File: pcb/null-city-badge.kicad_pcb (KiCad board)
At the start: 2 copper layers, 113.3 x 118.1 mm, 144 parts, among them J1 USB_C_Receptacle_USB2.0_16P, J10 Conn_01x10_Pin, J11 Conn_Coaxial_Small, J12 Conn_01x07_Pin, J2 Conn_01x02_Pin, J3 Conn_01x06_Pin, J4 Conn_01x24_Socket, J5 Conn_Coaxial_Small, J6 Conn_01x06_Pin, J7 Conn_01x06_Pin, J8 Conn_01x06_Pin, J9 Conn_01x10_Pin, Q1 SS8050, Q2 SS8050, Q3 IRLML0030, Q4 AO3401A, Q5 SS8050, U1 ESP32-S3-WROOM-1, U10 TCA9534, U11 CORE1262-868M, U12 ME6211C33M5, U13 CC1101RGP, U14 ME6211C33M5, U2 CP2102N-Axx-xQFN28, U3 SE050C2HQ1_Z01SDZ, U4 MCP73831-2-MC, U5 ME6211C33M5, U6 ME6211C33M5, U7 NS4168, U8 74125, U9 ME6211C33M5, Y2 26Mhz

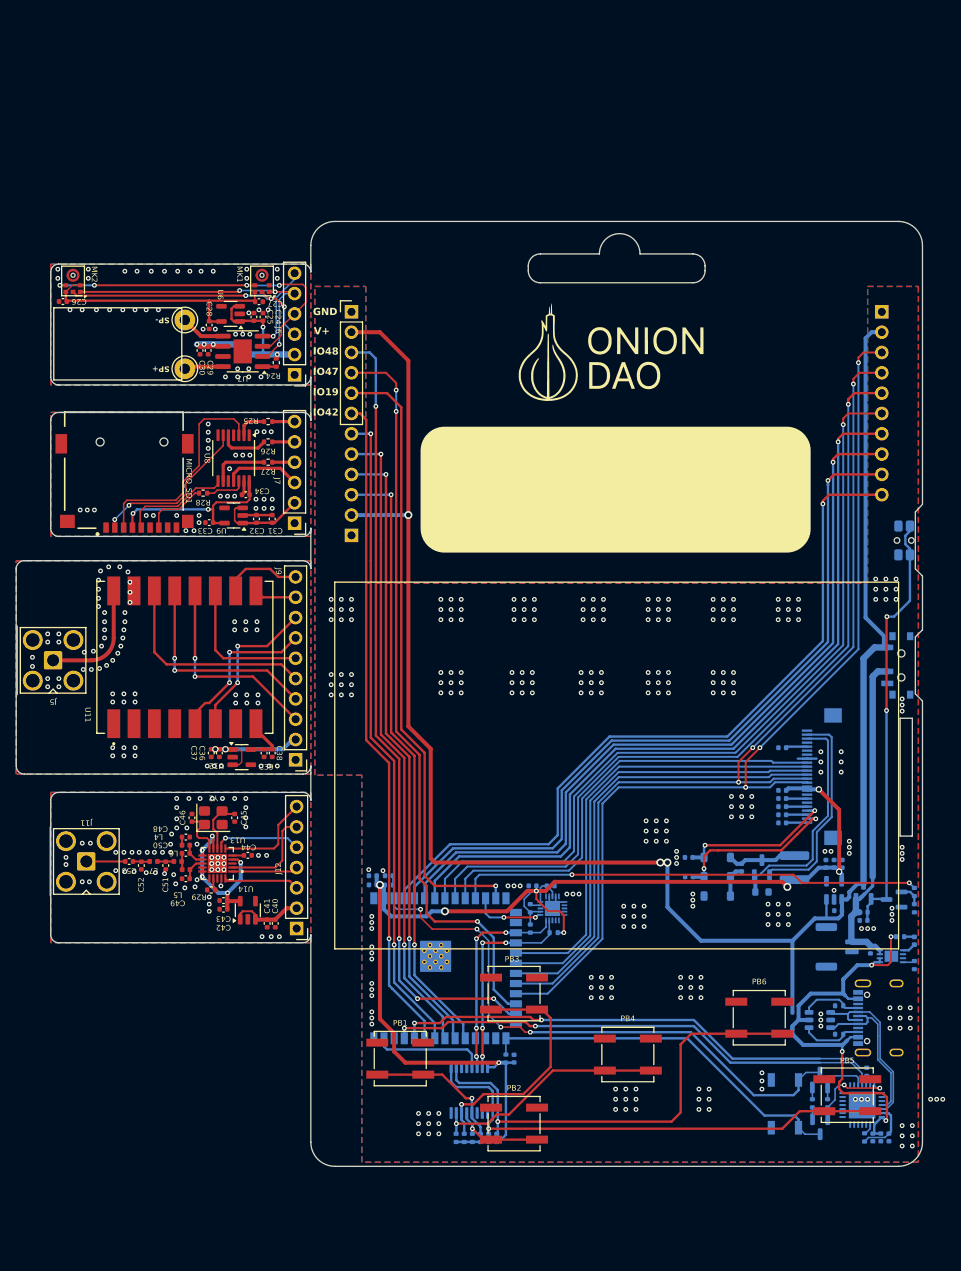
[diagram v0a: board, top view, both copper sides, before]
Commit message: feat: main board with sub ghz and audio modules, remove lora and sdcard
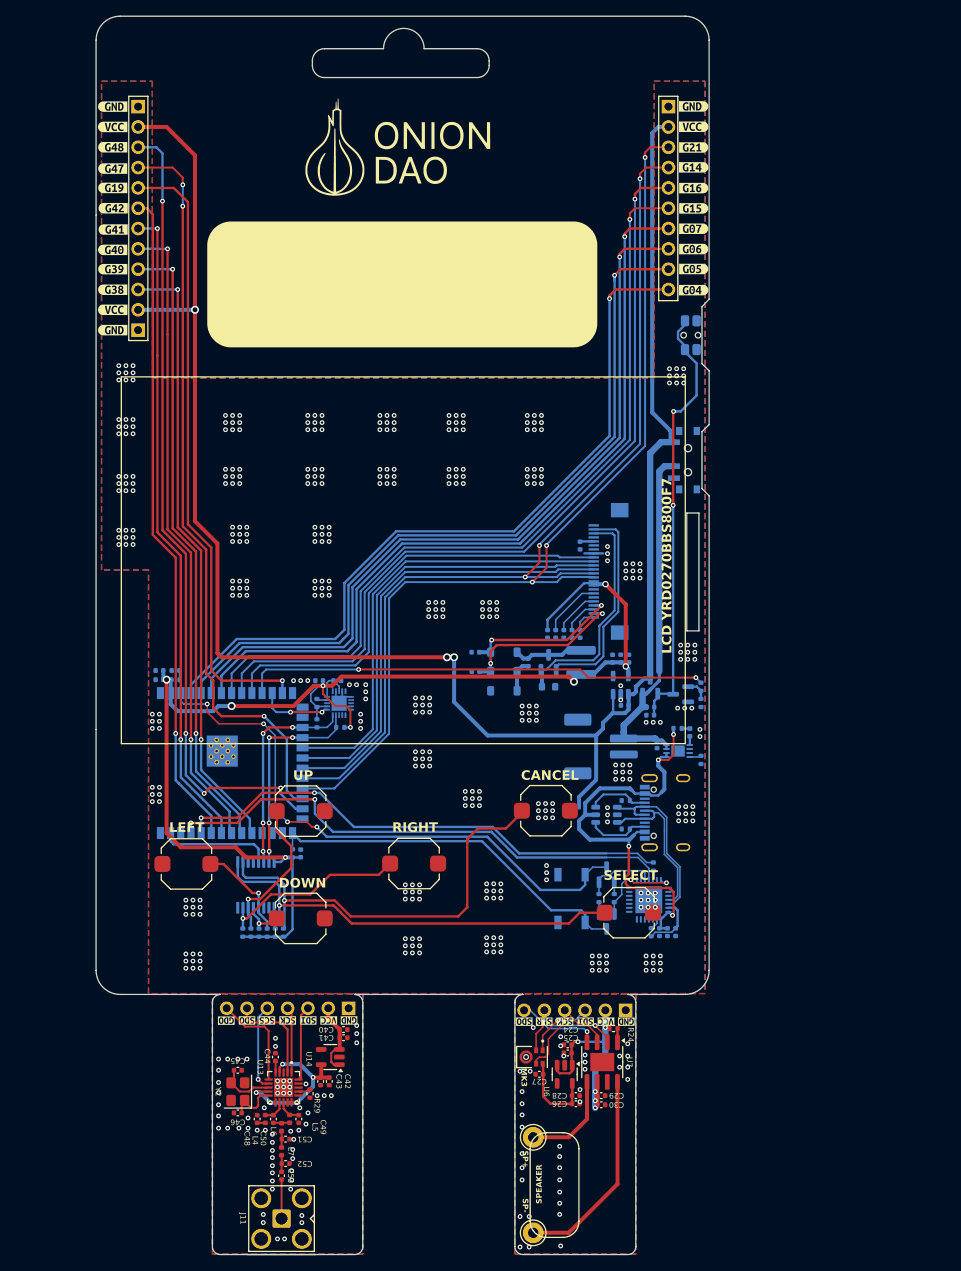
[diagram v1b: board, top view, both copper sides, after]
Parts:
- removed C31, C33, C36, C38: 10U, Capacitor_SMD:C_0402_1005Metric
- removed C32, C34, C37, C39: 100n, Capacitor_SMD:C_0402_1005Metric
- removed the G*** at (71.2, 89.4)
- removed the G*** at (74.4, 120.6)
- removed J5: Conn_Coaxial_Small, Connector_Coaxial:SMA_Amphenol_901-143_Horizontal
- removed J7: Conn_01x06_Pin, Connector_PinHeader_2.54mm:PinHeader_1x06_P2.54mm_Vertical
- removed J9: Conn_01x10_Pin, Connector_PinHeader_2.54mm:PinHeader_1x10_P2.54mm_Vertical
- removed MICRO_SD1: TF-01A, NIP_MOD:TF-01A
- removed MK1, MK2: ICS-43434, Sensor_Audio:InvenSense_ICS-43434-6_3.5x2.65mm
- removed R25, R26, R27, R28: R, Resistor_SMD:R_0402_1005Metric
- removed U11: CORE1262-868M, NIP_MOD:XCVR_CORE1262-868M
- removed U12, U9: ME6211C33M5, Package_TO_SOT_SMD:SOT-23-5
- removed U8: 74125, Package_SO:TSSOP-14_4.4x5mm_P0.65mm
- added G***: LOGO, NIP_LOGO:S_LOGO, B.Cu at (109.3, 56.0)
- added G***: LOGO, NIP_LOGO:S_LOGO_6, B.Cu at (125.6, 178.0)
- added G***: LOGO, NIP_LOGO:S_LOGO_6, B.Cu at (89.3, 173.5)
- added MK3: SPH0641LM4H-1, NIP_MOD:MIC_SPH0641LM4H-1, F.Cu at (123.7, 162.4)
- added kibuzzard-69D663AD: G***, kibuzzard-69D663AD, F.Cu at (144.6, 46.1)
- added kibuzzard-69D663C6: G***, kibuzzard-69D663C6, F.Cu at (144.6, 43.5)
- added kibuzzard-69D663C6: G***, kibuzzard-69D663C6, B.Cu at (72.0, 43.6)
- added kibuzzard-69D663C6: G***, kibuzzard-69D663C6, B.Cu at (136.1, 159.9)
- added kibuzzard-69D663C6: G***, kibuzzard-69D663C6, B.Cu at (72.0, 71.5)
- added kibuzzard-69D663C6: G***, kibuzzard-69D663C6, B.Cu at (101.4, 159.7)
- added kibuzzard-69D663D7: G***, kibuzzard-69D663D7, F.Cu at (144.6, 48.7)
- added kibuzzard-69D663E3: G***, kibuzzard-69D663E3, F.Cu at (144.6, 51.2)
- added kibuzzard-69D66402: G***, kibuzzard-69D66402, F.Cu at (144.6, 53.7)
- added kibuzzard-69D66408: G***, kibuzzard-69D66408, F.Cu at (144.6, 56.3)
- added kibuzzard-69D6643F: G***, kibuzzard-69D6643F, F.Cu at (144.6, 58.8)
- added kibuzzard-69D66453: G***, kibuzzard-69D66453, F.Cu at (144.6, 61.4)
- added kibuzzard-69D6645F: G***, kibuzzard-69D6645F, F.Cu at (144.6, 63.9)
- added kibuzzard-69D66465: G***, kibuzzard-69D66465, F.Cu at (144.6, 66.5)
- added kibuzzard-69D66565: G***, kibuzzard-69D66565, F.Cu at (72.0, 43.6)
- added kibuzzard-69D66565: G***, kibuzzard-69D66565, F.Cu at (72.0, 71.5)
- added kibuzzard-69D66565: G***, kibuzzard-69D66565, B.Cu at (144.6, 43.5)
- added kibuzzard-69D66580: G***, kibuzzard-69D66580, F.Cu at (72.0, 69.0)
- added kibuzzard-69D66580: G***, kibuzzard-69D66580, F.Cu at (72.0, 46.1)
- added kibuzzard-69D66580: G***, kibuzzard-69D66580, B.Cu at (144.6, 46.1)
- added kibuzzard-69D665BB: G***, kibuzzard-69D665BB, B.Cu at (144.6, 66.5)
- added kibuzzard-69D665D2: G***, kibuzzard-69D665D2, B.Cu at (144.6, 63.9)
- added kibuzzard-69D665E3: G***, kibuzzard-69D665E3, B.Cu at (144.6, 61.4)
- added kibuzzard-69D665EF: G***, kibuzzard-69D665EF, B.Cu at (144.6, 58.8)
- added kibuzzard-69D665FA: G***, kibuzzard-69D665FA, B.Cu at (144.6, 56.3)
- added kibuzzard-69D66608: G***, kibuzzard-69D66608, B.Cu at (144.6, 51.2)
- added kibuzzard-69D66615: G***, kibuzzard-69D66615, B.Cu at (144.6, 48.7)
- added kibuzzard-69D66624: G***, kibuzzard-69D66624, B.Cu at (144.6, 53.7)
- added kibuzzard-69D673B2: G***, kibuzzard-69D673B2, F.Cu at (72.0, 48.6)
- added kibuzzard-69D673C1: G***, kibuzzard-69D673C1, F.Cu at (72.0, 51.3)
- added kibuzzard-69D673C9: G***, kibuzzard-69D673C9, F.Cu at (72.0, 53.7)
- added kibuzzard-69D673D2: G***, kibuzzard-69D673D2, F.Cu at (72.1, 56.3)
- added kibuzzard-69D673D8: G***, kibuzzard-69D673D8, F.Cu at (72.1, 58.9)
- added kibuzzard-69D673DD: G***, kibuzzard-69D673DD, F.Cu at (72.0, 61.5)
- added kibuzzard-69D673E3: G***, kibuzzard-69D673E3, F.Cu at (72.0, 63.9)
- added kibuzzard-69D673EE: G***, kibuzzard-69D673EE, F.Cu at (72.0, 66.4)
- added kibuzzard-69D70112: G***, kibuzzard-69D70112, B.Cu at (98.9, 159.7)
- added kibuzzard-69D70112: G***, kibuzzard-69D70112, B.Cu at (133.6, 159.9)
- added kibuzzard-69D70112: G***, kibuzzard-69D70112, B.Cu at (72.0, 46.1)
- added kibuzzard-69D70126: G***, kibuzzard-69D70126, B.Cu at (72.0, 48.6)
- added kibuzzard-69D7012B: G***, kibuzzard-69D7012B, B.Cu at (72.0, 51.3)
- added kibuzzard-69D70130: G***, kibuzzard-69D70130, B.Cu at (72.0, 53.7)
- added kibuzzard-69D70134: G***, kibuzzard-69D70134, B.Cu at (72.1, 56.3)
- added kibuzzard-69D70141: G***, kibuzzard-69D70141, B.Cu at (72.1, 58.9)
- added kibuzzard-69D70146: G***, kibuzzard-69D70146, B.Cu at (72.0, 61.5)
- added kibuzzard-69D7014E: G***, kibuzzard-69D7014E, B.Cu at (72.0, 63.9)
- added kibuzzard-69D70154: G***, kibuzzard-69D70154, B.Cu at (72.0, 66.4)
- added kibuzzard-69D70186: G***, kibuzzard-69D70186, B.Cu at (72.0, 69.0)
- added kibuzzard-69D7A260: G***, kibuzzard-69D7A260, B.Cu at (88.7, 159.7)
- added kibuzzard-69D7A260: G***, kibuzzard-69D7A260, B.Cu at (123.4, 159.9)
- added kibuzzard-69D7A287: G***, kibuzzard-69D7A287, B.Cu at (128.5, 160.0)
- added kibuzzard-69D7A287: G***, kibuzzard-69D7A287, B.Cu at (93.8, 159.7)
- added kibuzzard-69D7A28C: G***, kibuzzard-69D7A28C, B.Cu at (131.1, 159.9)
- added kibuzzard-69D7A28C: G***, kibuzzard-69D7A28C, B.Cu at (96.3, 159.7)
- added kibuzzard-69D7A2FA: G***, kibuzzard-69D7A2FA, B.Cu at (126.0, 159.9)
- added kibuzzard-69D7A5EF: G***, kibuzzard-69D7A5EF, F.Cu at (125.9, 157.9)
- added kibuzzard-69D7A5F4: G***, kibuzzard-69D7A5F4, F.Cu at (123.5, 157.9)
- added kibuzzard-69D7A5F4: G***, kibuzzard-69D7A5F4, F.Cu at (88.8, 157.8)
- added kibuzzard-69D7A626: G***, kibuzzard-69D7A626, F.Cu at (93.9, 157.8)
- added kibuzzard-69D7A626: G***, kibuzzard-69D7A626, F.Cu at (128.5, 157.9)
- added kibuzzard-69D7A630: G***, kibuzzard-69D7A630, F.Cu at (96.5, 157.8)
- added kibuzzard-69D7A630: G***, kibuzzard-69D7A630, F.Cu at (131.1, 157.9)
- added kibuzzard-69D7A638: G***, kibuzzard-69D7A638, F.Cu at (99.0, 157.8)
- added kibuzzard-69D7A638: G***, kibuzzard-69D7A638, F.Cu at (133.7, 157.9)
- added kibuzzard-69D7A640: G***, kibuzzard-69D7A640, F.Cu at (136.2, 157.9)
- added kibuzzard-69D7A640: G***, kibuzzard-69D7A640, F.Cu at (101.6, 157.8)
- added kibuzzard-69D7D7AD: G***, kibuzzard-69D7D7AD, B.Cu at (86.2, 159.7)
- added kibuzzard-69D7D7BC: G***, kibuzzard-69D7D7BC, B.Cu at (91.2, 159.7)
- added kibuzzard-69D7D86C: G***, kibuzzard-69D7D86C, F.Cu at (91.3, 157.8)
- added kibuzzard-69D7D873: G***, kibuzzard-69D7D873, F.Cu at (86.2, 157.8)
- C2: value 1OOn -> 100n
- J12, J6: moved to B.Cu
- J2: footprint Connector_JST:JST_GH_SM02B-GHS-TB_1x02-1MP_P1.25mm_Horizontal -> Connector_JST:JST_PH_S2B-PH-SM4-TB_1x02-1MP_P2.00mm_Horizontal
- PB1, PB2, PB3, PB4, PB5, PB6: footprint Button_Switch_SMD:SW_SPST_B3SL-1002P -> Button_Switch_SMD:SW_Push_1TS009xxxx-xxxx-xxxx_6x6x5mm
- moved G*** 124.3 mm to (132.3, 179.0), turned to -90 degrees
- moved C26 119.0 mm to (129.9, 168.2), turned to 0 degrees
- moved TP1 116.5 mm to (124.6, 184.3)
- moved TP2 111.1 mm to (124.6, 172.4)
- moved C30 106.8 mm to (133.1, 168.3), turned to 0 degrees
- moved C28 106.7 mm to (129.9, 167.2), turned to 180 degrees
- moved C29 105.3 mm to (133.1, 167.2), turned to 0 degrees
- moved U6 103.8 mm to (128.5, 164.5), turned to -90 degrees
- moved C27 102.7 mm to (125.3, 164.5), turned to 180 degrees
- moved C25 100.0 mm to (128.9, 161.9), turned to 180 degrees
- moved U7 99.6 mm to (133.2, 163.0), turned to -90 degrees
- moved C24 98.6 mm to (128.9, 160.8), turned to 180 degrees
- moved R24 93.3 mm to (134.6, 158.8), turned to 180 degrees
- moved J6 89.6 mm to (136.1, 156.5), turned to 90 degrees
- moved J11 50.9 mm to (93.1, 182.6), turned to 180 degrees
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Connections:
- net /CS_4 renamed /CC1101 MODULE/CS_4
- net /GDO renamed /CC1101 MODULE/GDO
- net /SCK_1 renamed /SOUND MODULE/SCK_1
- net /SCK_4 renamed /CC1101 MODULE/SCK_4
- net /SDI_4 renamed /CC1101 MODULE/SDI_4
- net /SDO_1 renamed /SOUND MODULE/SDO_1
- net /SDO_4 renamed /CC1101 MODULE/SDO_4
- net /WS_1 renamed /SOUND MODULE/WS_1
- BOOT1 pad 1: GND -> GND1
- C1 pad 2: GND -> GND1
- C10 pad 2: GND -> GND1
- C11 pad 2: GND -> GND1
- C13 pad 1: GND -> GND1
- C14 pad 1: GND -> GND1
- C15 pad 1: GND -> GND1
- C16 pad 1: GND -> GND1
- C17 pad 1: GND -> GND1
- C18 pad 1: GND -> GND1
- C19 pad 1: GND -> GND1
- C2 pad 2: GND -> GND1
- C20 pad 2: GND -> GND1
- C21 pad 1: GND -> GND1
- C22 pad 1: GND -> GND1
- C23 pad 1: GND -> GND1
- C3 pad 2: GND -> GND1
- C35 pad 1: GND -> GND1
- C4 pad 2: GND -> GND1
- C5 pad 2: GND -> GND1
- C6 pad 2: GND -> GND1
- C7 pad 2: GND -> GND1
- C8 pad 2: GND -> GND1
- C9 pad 2: GND -> GND1
- D1 pad 2: GND -> GND1
- D7 pad 1: GND -> GND1
- J1 pad A1: GND -> GND1
- J1 pad A12: GND -> GND1
- J1 pad B1: GND -> GND1
- J1 pad B12: GND -> GND1
- J1 pad S1: GND -> GND1
- J10 pad 1: GND -> GND1
- J2 pad 1: GND -> GND1
- J3 pad 1: GND -> GND1
- J4 pad 8: GND -> GND1
- J6 pad 3: /SDI_1 -> /SOUND MODULE/SDI_1
- J8 pad 1: GND -> GND1
- ON/OFF_PB1 pad 1: GND -> Net-(Q4-G)
- ON/OFF_PB1 pad 2: Net-(Q4-G) -> GND1
- PB1 pad 1: GND -> GND1
- PB2 pad 1: GND -> GND1
- PB3 pad 1: GND -> GND1
- PB4 pad 1: GND -> GND1
- PB5 pad 1: GND -> GND1
- PB6 pad 1: GND -> GND1
- Q5 pad 2: GND -> GND1
- R20 pad 1: GND -> GND1
- R23 pad 2: GND -> GND1
- R4 pad 2: GND -> GND1
- R5 pad 2: GND -> GND1
- R6 pad 1: GND -> GND1
- RST1 pad 1: GND -> GND1
- U1 pad 1: GND -> GND1
- U1 pad 40: GND -> GND1
- U1 pad 41: GND -> GND1
- U10 pad 1: GND -> GND1
- U10 pad 2: GND -> GND1
- U10 pad 3: GND -> GND1
- U10 pad 8: GND -> GND1
- U2 pad 29: GND -> GND1
- U2 pad 3: GND -> GND1
- U3 pad 1: GND -> GND1
- U3 pad 17: GND -> GND1
- U3 pad 19: GND -> GND1
- U3 pad 21: GND -> GND1
- U4 pad 6: GND -> GND1
- U4 pad 9: GND -> GND1
- U5 pad 2: GND -> GND1
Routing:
- net /SDI_1: track 32.7 -> 0.00 mm, vias 3 -> 0
- net /SOUND MODULE/SCK_1: track 42.9 -> 14.9 mm, vias 4 -> 0
- net /SDO_L: track 27.3 -> 0.00 mm
- net /CS_3: track 26.7 -> 0.00 mm
- net /SCK_3: track 26.6 -> 0.00 mm, vias 2 -> 0
- net /SDI_3: track 25.5 -> 0.00 mm, vias 2 -> 0
- net 3V3_2: track 22.8 -> 0.00 mm, vias 2 -> 0
- net /SOUND MODULE/WS_1: track 38.8 -> 16.5 mm, vias 3 -> 1
- net 3V3_1: track 32.4 -> 10.7 mm
- net Net-(U7-VOP): track 4.87 -> 25.8 mm
- net /CS_L: track 20.5 -> 0.00 mm, vias 2 -> 0
- net /DIO2_: track 20.0 -> 0.00 mm, vias 2 -> 0
- net /DIO1_: track 19.5 -> 0.00 mm, vias 2 -> 0
- net /SDO_3: track 17.9 -> 0.00 mm
- net VSYS_3: track 17.0 -> 0.00 mm, vias 2 -> 0
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- added copper zone on B.Cu, net GND1
- added copper zone on F.Cu, net GND1
- removed copper zone on B.Cu, net GND
- removed copper zone on F.Cu, net GND
- removed copper zone on B.Cu, net GND_2
- removed copper zone on F.Cu, net GND_2
- removed copper zone on B.Cu, net GND_3
- removed copper zone on F.Cu, net GND_3
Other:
- board size 113.3 x 118.1 mm -> 76.6 x 154.8 mm
- board text added: "BAT+"
- board text added: "BAT-"
- board text added: "BATTERY"
- board text added: "CANCEL"
- board text added: "DEVELOPED BY SKYRIZZ"
- board text added: "DOWN"
- board text added: "LCD YRD0270BBS800F7"
- board text added: "LEFT"
- board text added: "RIGHT"
- board text added: "SELECT"
- board text added: "SPEAKER"
- board text added: "UP"
- board text removed: "BSY"
- board text removed: "CS"
- board text removed: "DIO1"
- board text removed: "DIO2"
- board text removed: "Developed by SKYRIZZ"
- board text removed: "GDO"
- board text removed: "GND"
- board text removed: "IO14"
- board text removed: "IO15"
- board text removed: "IO16"
- board text removed: "IO19"
- board text removed: "IO21"
- board text removed: "IO38"
- board text removed: "IO39"
- board text removed: "IO4"
- board text removed: "IO40"
- board text removed: "IO41"
- board text removed: "IO42"
- board text removed: "IO47"
- board text removed: "IO48"
- board text removed: "IO5"
- board text removed: "IO6"
- board text removed: "IO7"
- board text removed: "RST"
- board text removed: "SCK"
- board text removed: "SCK/BCLK"
- board text removed: "SDI"
- board text removed: "SDO"
- board text removed: "V+"
- board text removed: "WS/LRCLK"
